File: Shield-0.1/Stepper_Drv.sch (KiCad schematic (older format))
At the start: 66 parts, among them J17 VREF, J3 VREF, U5 A4982SLPTR, U7 A4982SLPTR, U9 MCP44X1

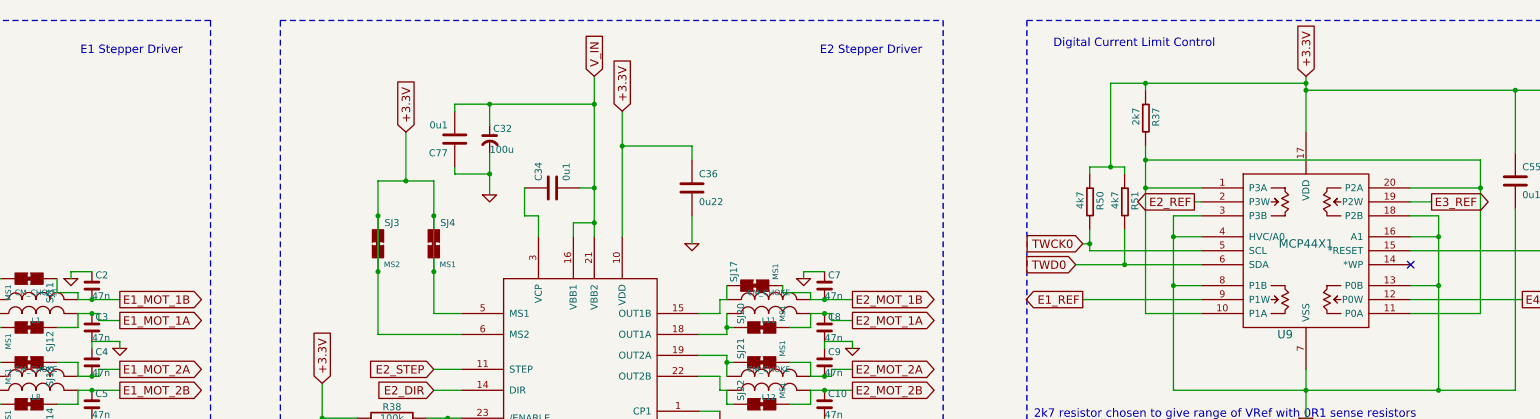
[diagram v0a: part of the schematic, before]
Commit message: Corrected the address of the digital potentiometer on the Shield.  It is now the same as the expansion board.  Also removed the pullup resistors on Shield lines TWCK0 and TWD0 as there are pullups on the main board.
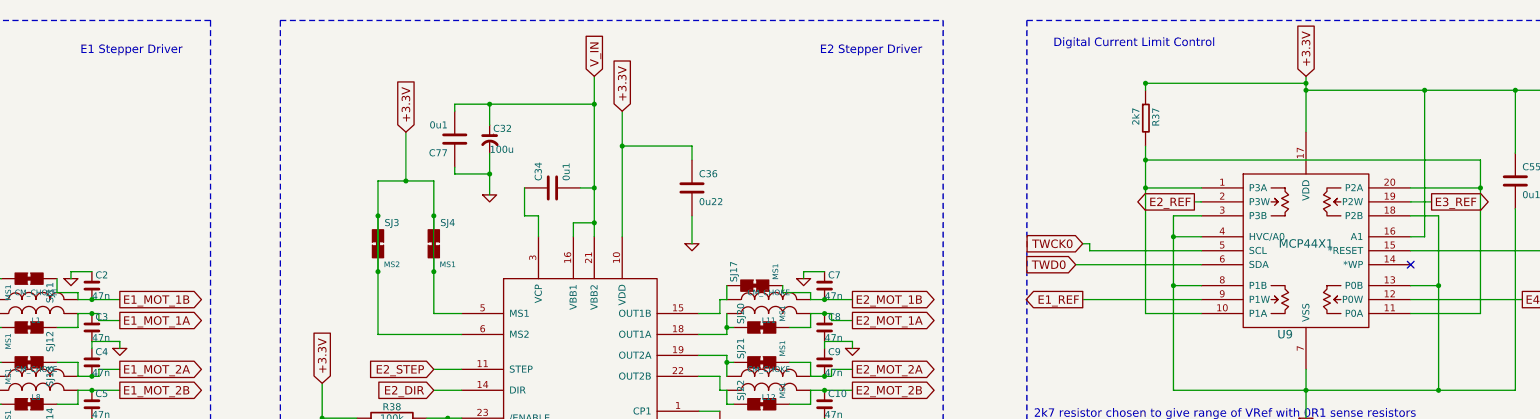
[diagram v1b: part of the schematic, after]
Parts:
- removed R50, R51: 4k7, symbol R_SMALL
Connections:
- net +3.3V: now also U9.16 (A1)
- net GND: no longer U9.16 (A1)
